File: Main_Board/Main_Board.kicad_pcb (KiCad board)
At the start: 2 copper layers, 99 x 70 mm, 20 parts, among them P1 CONN_02X04, P2 CONN_02X04, P3 CONN_01X03, P5 CONN_02X12, U1 TLV1117LV33, U2 DYS_mini_ESC, U3 DYS_mini_ESC, U4 DYS_mini_ESC, U5 DYS_mini_ESC, U6 TENDA_P200

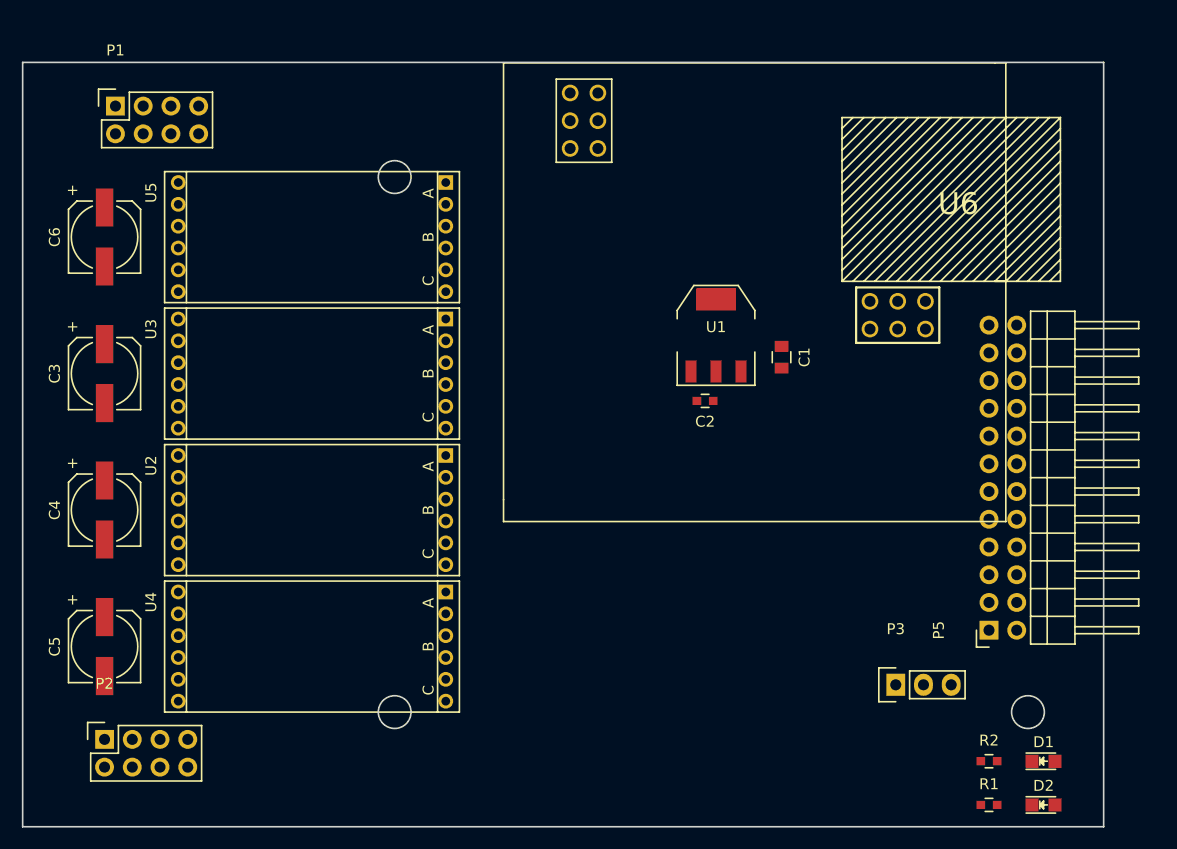
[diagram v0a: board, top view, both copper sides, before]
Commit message: Main Board : Add Braket Hole
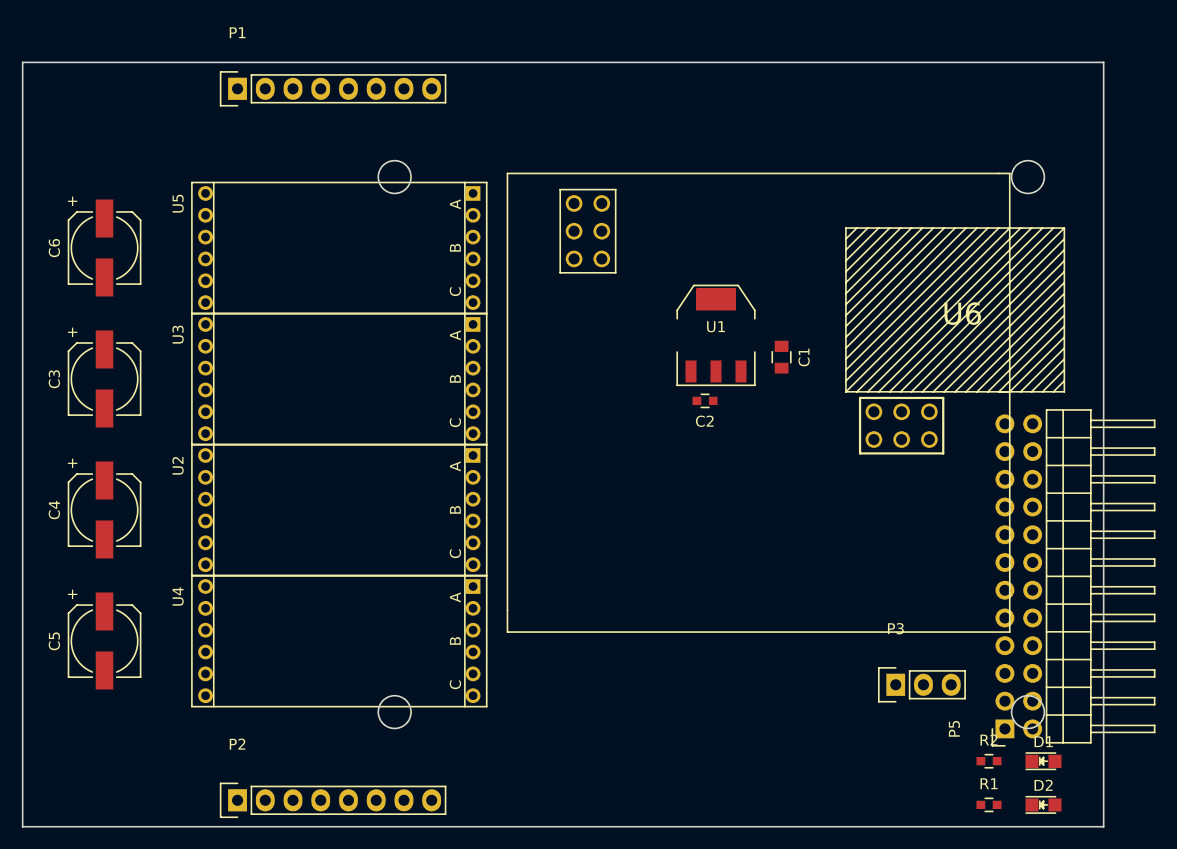
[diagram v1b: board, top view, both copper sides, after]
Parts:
- P1, P2: value CONN_02X04 -> CONN_01X08; footprint Socket_Strips:Socket_Strip_Straight_2x04 -> Socket_Strips:Socket_Strip_Straight_1x08
- moved P2 13.4 mm to (70.2, 132.6)
- moved P1 11.3 mm to (70.2, 67.4)
- moved U6 10.1 mm to (117.4, 96.1)
- moved P5 9.16 mm to (140.5, 126.0)
- moved U5 2.69 mm to (79.5, 82.0)
- moved U3 2.55 mm to (79.5, 94.0)
- moved U4 2.55 mm to (79.5, 118.0)
- moved U2 2.50 mm to (79.5, 106.0)
- moved C6 1.00 mm to (58.0, 82.0)
- moved C3 0.50 mm to (58.0, 94.0)
- moved C5 0.50 mm to (58.0, 118.0)
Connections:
- P1 pad 2: GND -> /CH1
- P1 pad 3: /CH1 -> /CH3
- P1 pad 4: /CH2 -> /CH5
- P1 pad 5: /CH3 -> /CH6
- P1 pad 7: /CH5 -> /CH2
- P1 pad 8: /CH6 -> GND
- P2 pad 2: /SCL -> (no net)
- P2 pad 4: /SDA -> (no net)
- P2 pad 5: (no net) -> /SCL
- P2 pad 6: (no net) -> /SDA
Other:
- outline, holes or cut-outs redrawn

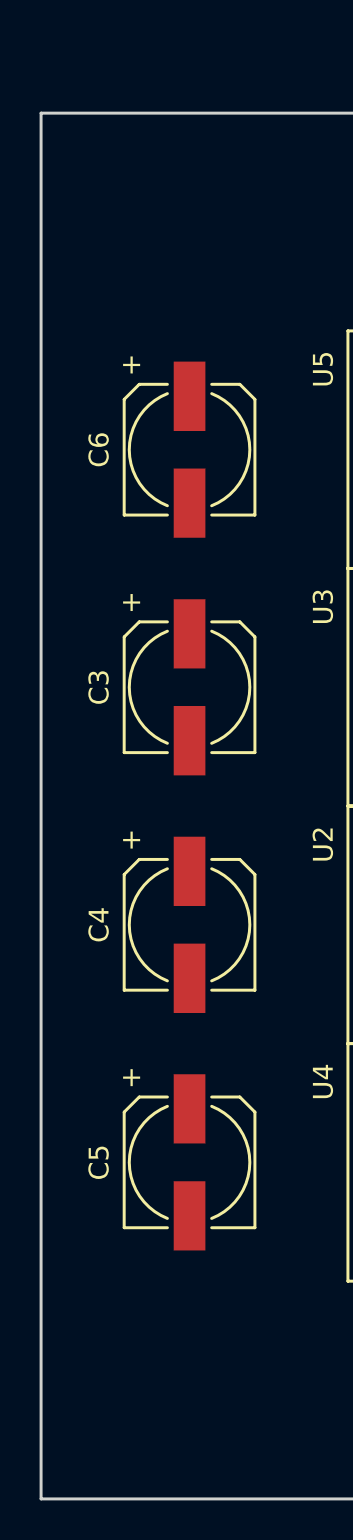
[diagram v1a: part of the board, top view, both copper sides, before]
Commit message: Main Board & USB Board : Edit EdgeCuts
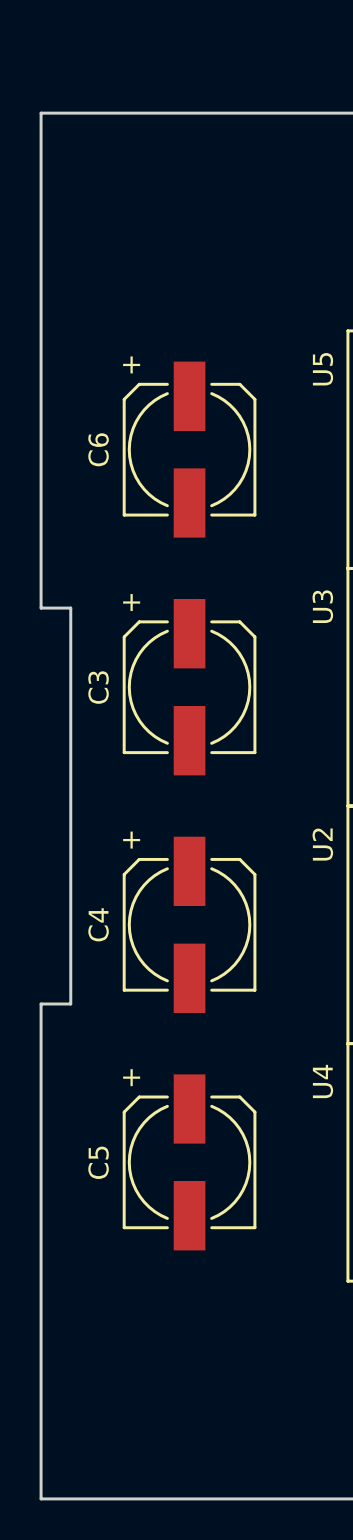
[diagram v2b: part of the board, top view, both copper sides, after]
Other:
- outline, holes or cut-outs redrawn
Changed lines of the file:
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@@
     (links 90)
     (no_connects 90)
-    (area 50.424999 64.924999 149.575001 135.075001)
+    (area 50.399999 61.345 154.685001 135.975)
     (thickness 1.6)
-    (drawings 10)
+    (drawings 14)
     (tracks 0)
     (zones 0)
@@
     )
   )
+  (gr_line (start 50.5 110) (end 50.5 135) (layer Edge.Cuts) (width 0.15))
+  (gr_line (start 50.5 110) (end 52 110) (layer Edge.Cuts) (width 0.15))
+  (gr_line (start 52 90) (end 52 110) (layer Edge.Cuts) (width 0.15))
+  (gr_line (start 50.5 90) (end 52 90) (layer Edge.Cuts) (width 0.15))
   (gr_circle (center 142.57 75.5) (end 142.57 77) (layer Edge.Cuts) (width 0.15))
   (gr_line (start 50.5 75.27) (end 65 75.27) (layer B.Paste) (width 0.2))
@@
   (gr_circle (center 84.57 124.5) (end 84.57 126) (layer Edge.Cuts) (width 0.15))
   (gr_circle (center 142.57 124.5) (end 142.57 126) (layer Edge.Cuts) (width 0.15))
-  (gr_line (start 50.5 65) (end 50.5 135) (layer Edge.Cuts) (width 0.15))
+  (gr_line (start 50.5 65) (end 50.5 90) (layer Edge.Cuts) (width 0.15))
   (gr_line (start 50.5 135) (end 149.5 135) (layer Edge.Cuts) (width 0.15))
   (gr_line (start 149.5 65) (end 149.5 135) (layer Edge.Cuts) (width 0.15))

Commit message: Main Board incomplete routing
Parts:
- moved R1 67.1 mm to (159.0, 69.0)
- moved D1 65.8 mm to (163.0, 66.0)
- moved D2 64.2 mm to (164.0, 72.0)
- moved R2 57.2 mm to (157.8, 75.0)
- moved U5 36.0 mm to (79.5, 118.0)
- moved U2 24.0 mm to (79.5, 82.0)
- moved U4 12.0 mm to (79.5, 106.0)
- moved P5 4.27 mm to (143.5, 129.1)
- moved U6 1.46 mm to (118.8, 96.0)
- turned C3 to 180 degrees
- turned C4 to 180 degrees
- turned C5 to 180 degrees
- turned C6 to 180 degrees
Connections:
- P1 pad 2: /CH1 -> GND
- P1 pad 3: /CH3 -> /CH2
- P1 pad 4: /CH5 -> /CH1
- P1 pad 5: /CH6 -> /CH4
- P1 pad 6: /CH4 -> /CH3
- P1 pad 7: /CH2 -> /CH6
- P1 pad 8: GND -> /CH5
- P2 pad 2: (no net) -> GND
- P2 pad 3: (no net) -> /SDA
- P2 pad 6: /SDA -> (no net)
- P2 pad 7: (no net) -> GND
- P2 pad 8: GND -> (no net)
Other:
- outline, holes or cut-outs redrawn
- board text added: "ESC1"
- board text added: "ESC2"
- board text added: "ESC3"
- board text added: "ESC4"

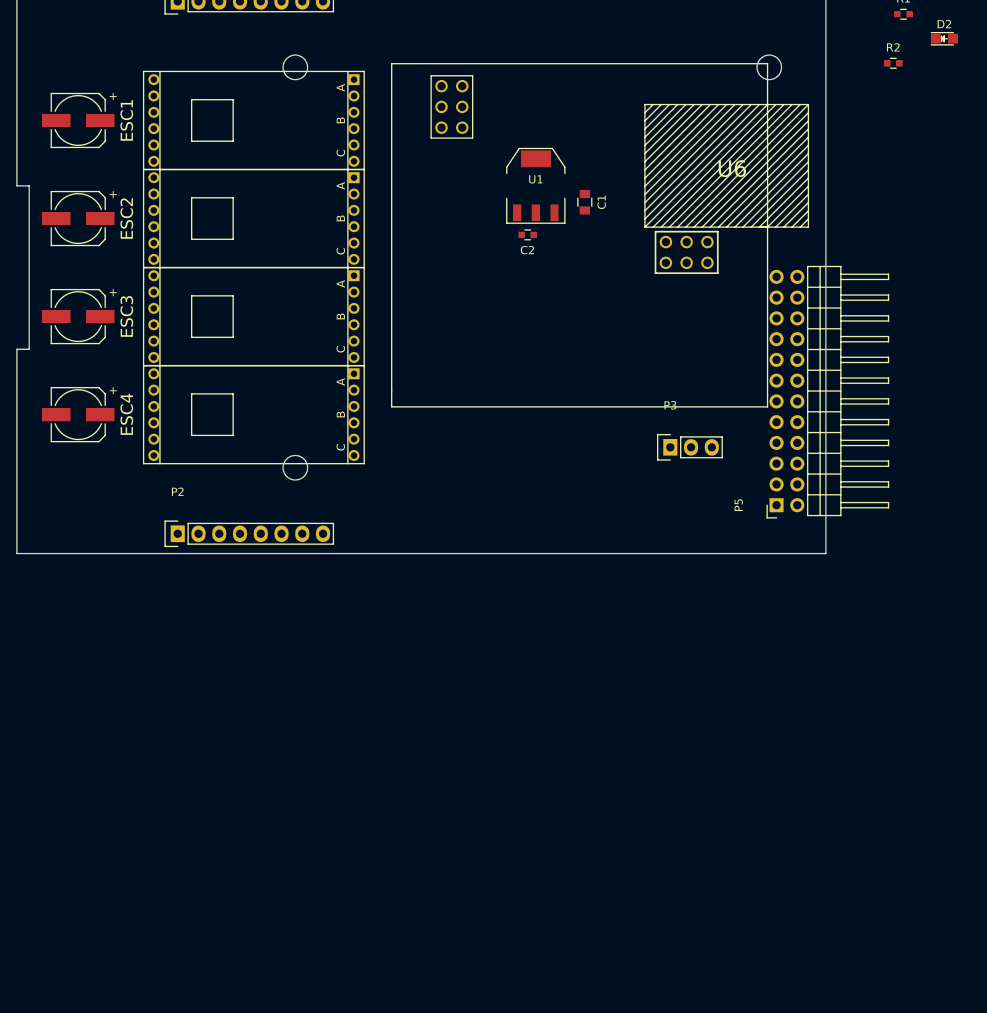
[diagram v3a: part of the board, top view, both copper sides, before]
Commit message: Main Board : Separate PCB into two part
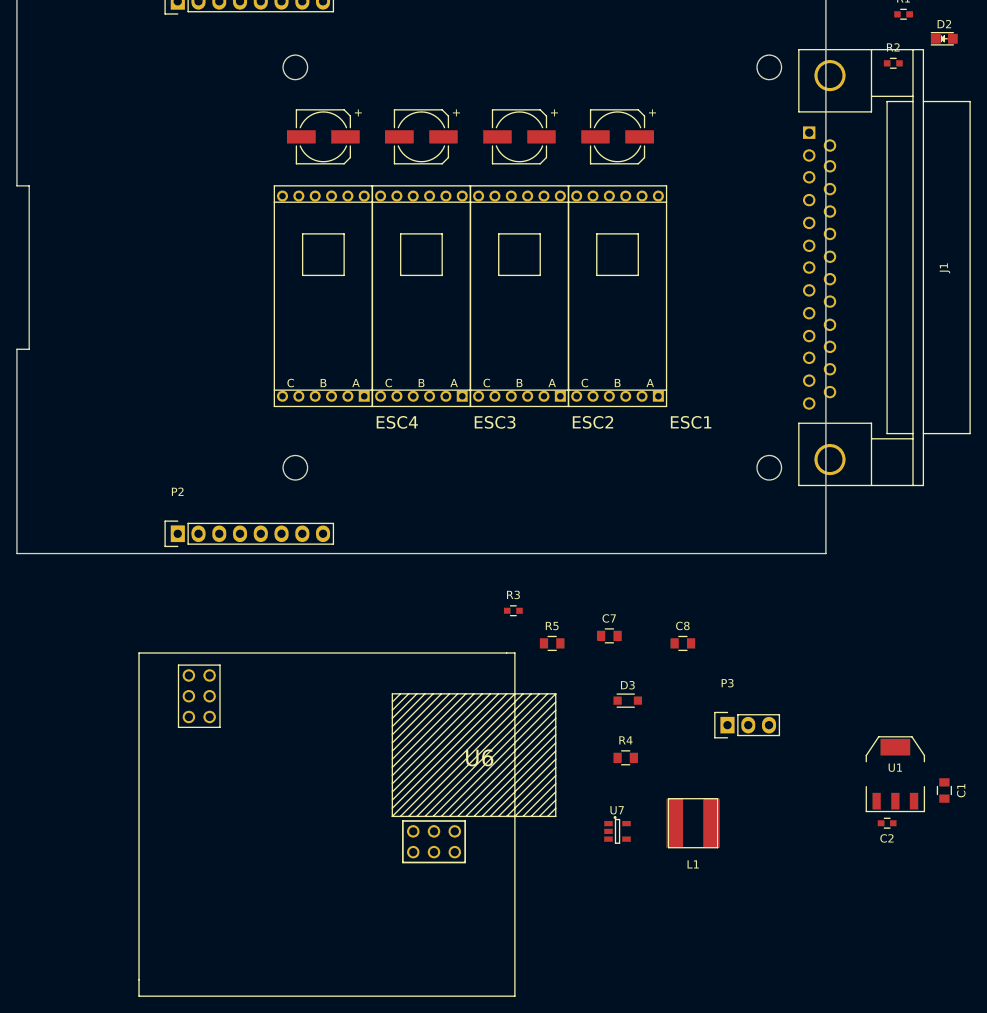
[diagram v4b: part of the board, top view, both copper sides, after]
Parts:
- removed P5: CONN_02X12, KiCad_Footprint:Socket_Strip_Angled_2x12
- added C7: 1uF, Capacitors_SMD:C_0805, F.Cu at (123.0, 145.1)
- added C8: 2.2uF, Capacitors_SMD:C_0805, F.Cu at (132.0, 146.0)
- added D3: BAT20JFILM, Diodes_SMD:SOD-323_HandSoldering, F.Cu at (125.2, 153.0)
- added J1: DB25, Connect:DB25FC, F.Cu at (148.7, 100.0)
- added L1: 33uH, KiCad_Footprint:inductor_33uH, F.Cu at (133.2, 168.0)
- added R3: 10k, Capacitors_SMD:C_0603, F.Cu at (111.2, 142.0)
- added R4: 0.5, Capacitors_SMD:C_0805, F.Cu at (125.0, 160.0)
- added R5: 0.5, Capacitors_SMD:C_0805, F.Cu at (116.0, 146.0)
- added U7: AL8805W5, TO_SOT_Packages_SMD:SOT-23-5, F.Cu at (124.0, 169.0)
- moved C1 84.4 mm to (164.0, 164.0)
- moved C2 84.4 mm to (157.0, 168.0)
- moved U1 84.4 mm to (158.0, 162.0)
- moved U6 78.5 mm to (87.9, 168.1)
- moved C3 66.8 mm to (124.0, 84.0)
- moved C4 58.3 mm to (112.0, 84.0)
- moved C5 54.0 mm to (100.0, 84.0)
- moved U2 49.4 mm to (124.0, 103.5), turned to 180 degrees
- moved P3 34.7 mm to (137.5, 156.0)
- moved U3 33.9 mm to (112.0, 103.5), turned to 180 degrees
- moved C6 30.1 mm to (88.0, 84.0)
- moved U4 20.7 mm to (100.0, 103.5), turned to 180 degrees
- moved U5 16.8 mm to (88.0, 103.5), turned to 180 degrees
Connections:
- net /CH1 renamed /Bottom_Board/CH1
- net /CH2 renamed /Bottom_Board/CH2
- net /CH3 renamed /Bottom_Board/CH3
- net /CH4 renamed /Bottom_Board/CH4
- net /V_BAT renamed /Bottom_Board/V_BAT
- C3 pad 2: GND -> /Bottom_Board/L_GND
- C4 pad 2: GND -> /Bottom_Board/L_GND
- C5 pad 2: GND -> /Bottom_Board/L_GND
- C6 pad 2: GND -> /Bottom_Board/L_GND
- P1 pad 2: GND -> /Bottom_Board/L_GND
- P1 pad 7: /CH6 -> (no net)
- P1 pad 8: /CH5 -> /Bottom_Board/CH5
- P2 pad 2: GND -> /Bottom_Board/L_GND
- P2 pad 3: /SDA -> (no net)
- P2 pad 5: /SCL -> (no net)
- P2 pad 7: GND -> /Bottom_Board/L_GND
- U2 pad 1: GND -> /Bottom_Board/L_GND
- U2 pad 4: /MOTOR_1A -> /Bottom_Board/MOTOR_1A
- U2 pad 5: /MOTOR_1B -> /Bottom_Board/MOTOR_1B
- U2 pad 6: /MOTOR_1C -> /Bottom_Board/MOTOR_1C
- U3 pad 1: GND -> /Bottom_Board/L_GND
- U3 pad 4: /MOTOR_2A -> /Bottom_Board/MOTOR_2A
- U3 pad 5: /MOTOR_2B -> /Bottom_Board/MOTOR_2B
- U3 pad 6: /MOTOR_2C -> /Bottom_Board/MOTOR_2C
- U4 pad 1: GND -> /Bottom_Board/L_GND
- U4 pad 4: /MOTOR_3A -> /Bottom_Board/MOTOR_3A
- U4 pad 5: /MOTOR_3B -> /Bottom_Board/MOTOR_3B
- U4 pad 6: /MOTOR_3C -> /Bottom_Board/MOTOR_3C
- U5 pad 1: GND -> /Bottom_Board/L_GND
- U5 pad 4: /MOTOR_4A -> /Bottom_Board/MOTOR_4A
- U5 pad 5: /MOTOR_4B -> /Bottom_Board/MOTOR_4B
- U5 pad 6: /MOTOR_4C -> /Bottom_Board/MOTOR_4C
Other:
- outline, holes or cut-outs redrawn
